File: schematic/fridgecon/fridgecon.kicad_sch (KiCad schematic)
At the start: 3 parts, among them J1 ICSPI, J2 MAX7219, U1 PIC12F675-xP

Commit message: v1.0.0
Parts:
- removed J2: MAX7219, symbol Connector:Conn_01x05_Socket
- added C1: 100n, symbol Device:C
- added D1: 2.2V, symbol Device:D_Zener
- added D2, D3, D5: LED, symbol Device:LED
- added D4: 1N4148, Diode_THT:D_DO-35_SOD27_P7.62mm_Horizontal, symbol Diode:1N4148
- added J2: Motor, symbol Connector:Screw_Terminal_01x02
- added J3: 220V~ IN, symbol Connector:Screw_Terminal_01x02
- added K1: 250V10A, Relay_THT:Relay_SPST-NO_Fujitsu_FTR-LYAA005x_FormA_Vertical, symbol Relay:Fujitsu_FTR-LYAA005x
- added Q1: PNP, symbol Simulation_SPICE:PNP
- added R1, R4: 100, symbol Device:R_US
- added R10, R12, R2, R3, R8, R9: 1K, symbol Device:R_US
- added R11, R6: 44.2K, symbol Device:R_US
- added R5: 220, symbol Device:R_US
- added R7: 13K, symbol Device:R_US
- added RV1: R_Potentiometer_US, symbol Device:R_Potentiometer_US
- added SW1: Tune, symbol Switch:SW_Push
- added U2: LM35-LP, Package_TO_SOT_THT:TO-92_Inline, symbol Sensor_Temperature:LM35-LP
- J1: value ICSPI -> ICSP
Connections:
- net +5V: now also Q1.3 (E), R5.1
- net Relay: now reaches U1.3 (GP4)
- net Relay: now also R9.2
- net Sensor: now reaches U1.5 (GP2)
- net Sensor: now also R3.1, R4.1
- net CS renamed Motor Status
- net Motor Status: now also R8.1
- net Clock renamed PGCLK
- net PGCLK: now also R6.2, R7.1
- net Data renamed PGDATA
- net GND: no longer names the net of U1.8 (VSS)
- net GND: no longer J1.3 (Pin_3)
- net VPP renamed Tune Feedback
- net Tune Feedback: now also R12.1
- new net: D5.2 (A), R12.2
- new net: D1.1 (K), R5.2, R6.1
- new net: C1.1, U2.1 (+V_{S})
- new net: C1.2, R1.2, R2.2
- new net: Q1.2 (B), R9.1
- new net: D2.2 (A), R8.2
- new net: J2.2 (Pin_2), K1.13
- new net: J3.1 (Pin_1), K1.14
- new net: D4.1 (K), K1.A1, Q1.1 (C), R10.1
- new net: D3.1 (K), D4.2 (A), K1.A2
- new net: J2.1 (Pin_1), J3.2 (Pin_2)
- new net: D1.2 (A), R7.2
- new net: R3.2, R4.2
- new net: D3.2 (A), R10.2
- new net: R1.1, U2.2 (V_{OUT})
- new net: R2.1, U2.3 (GND)
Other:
- note added: "ICSP"
- note added: "MCU"
- note added: "Relay"
- note added: "Sensor"
- note added: "User Interface"
- note added: "Voltage Reference"
- moved on the sheet: U1

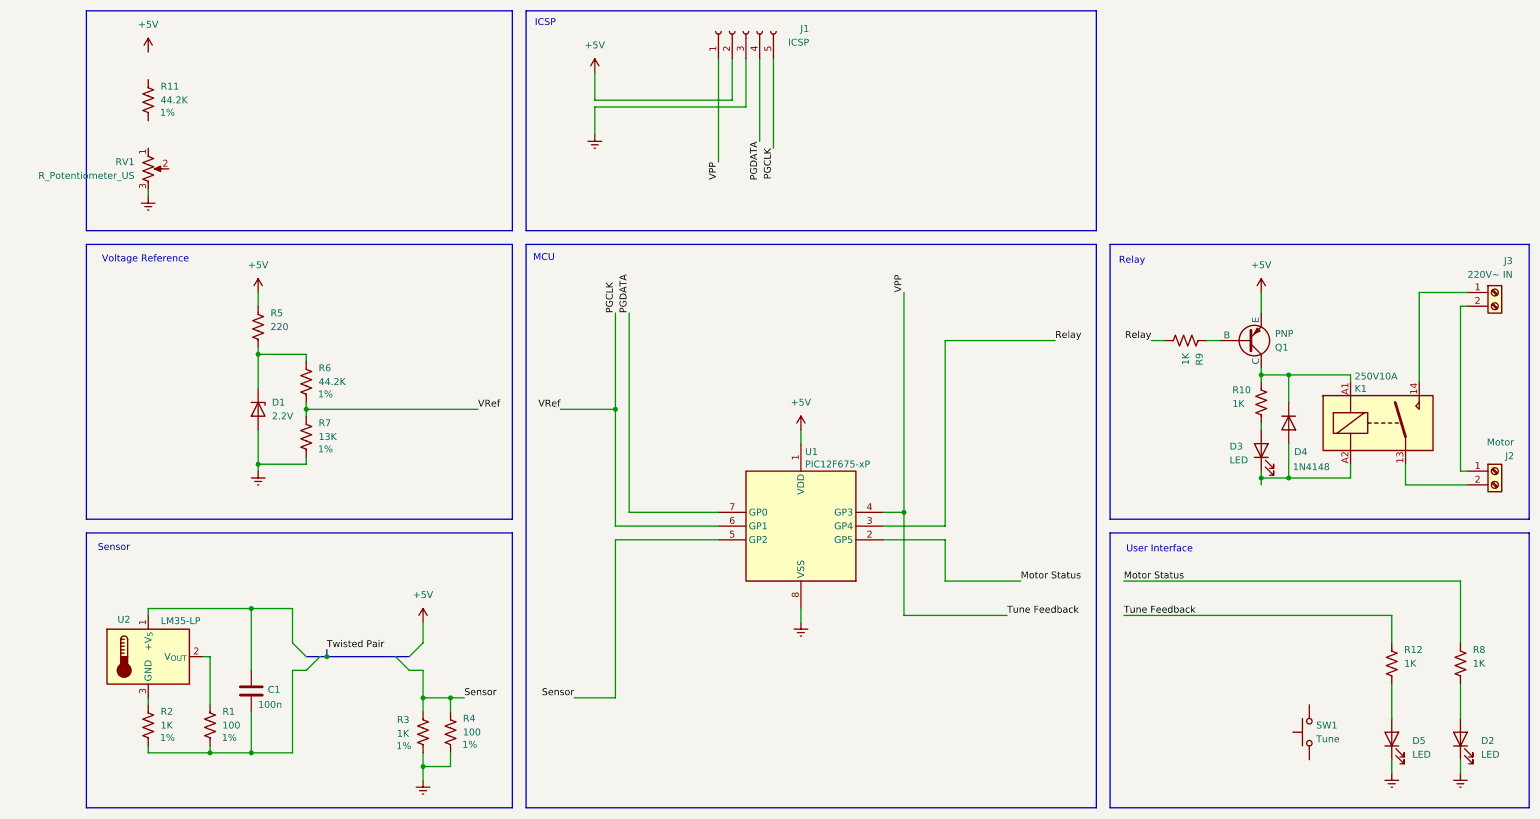
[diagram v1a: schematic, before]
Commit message: feature: GP2/INT
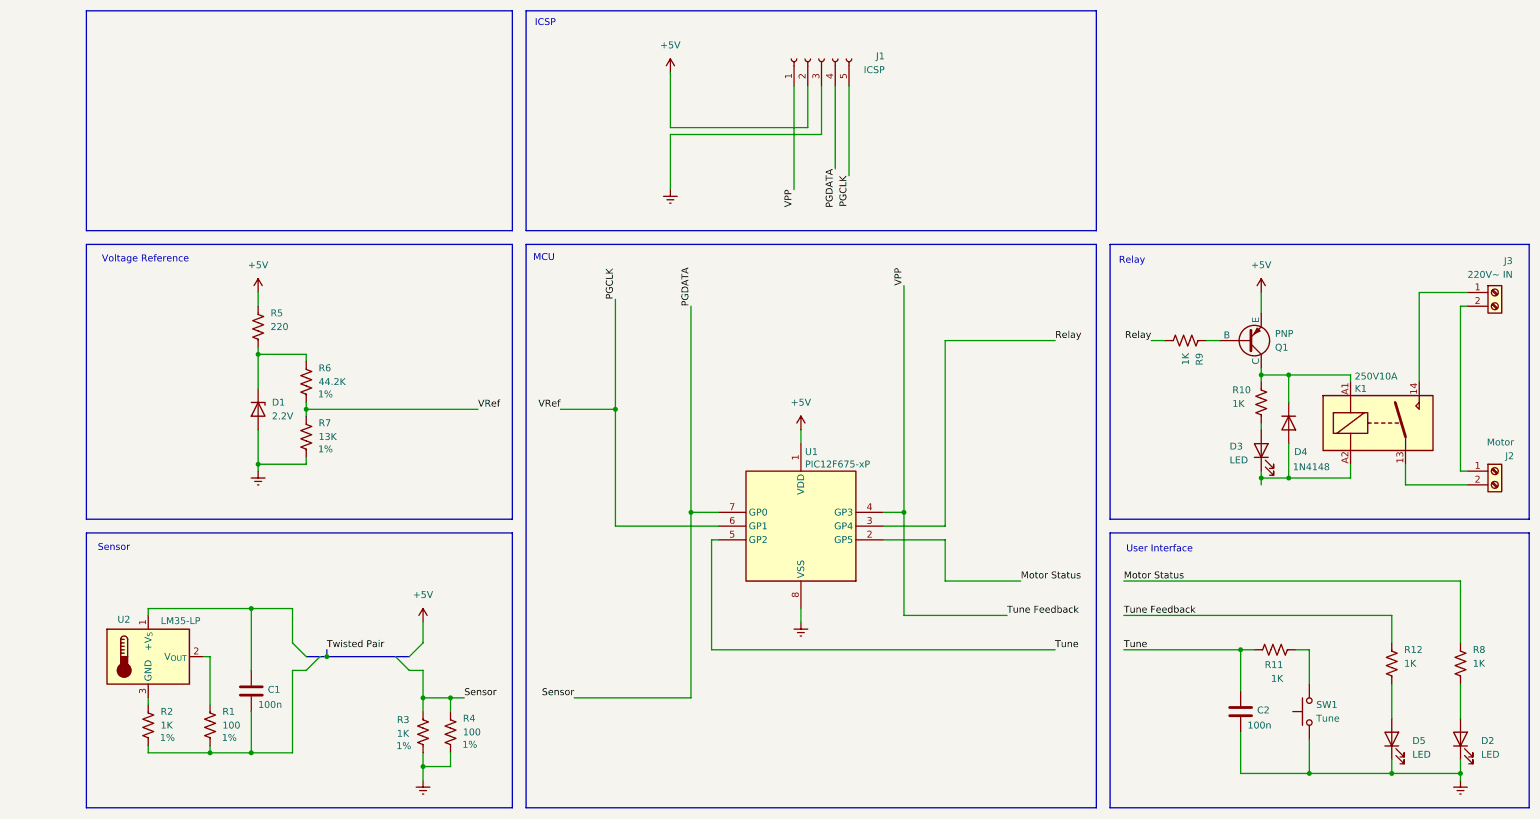
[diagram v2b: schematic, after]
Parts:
- removed RV1: R_Potentiometer_US, symbol Device:R_Potentiometer_US
- added C2: 100n, symbol Device:C
- R11: value 44.2K -> 1K
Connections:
- net PGDATA: now also R3.1, R4.1
- net Tune: now reaches R11.1
- net Tune: now also U1.5 (GP2), C2.1
- net at R11.2: now also SW1.2
- net at D5.1 (K): now also D2.1 (K), SW1.1, C2.2
- removed net Sensor: R3.1, R4.1, U1.5 (GP2)
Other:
- moved on the sheet: J1, SW1

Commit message: Feature: watchdog time
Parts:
- removed D5: LED, symbol Device:LED
- removed R12: 1K, symbol Device:R_US
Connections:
- net Tune Feedback is gone; now on net Tune: J1.1 (Pin_1), U1.4 (GP3)
- net PGDATA: no longer R3.1, R4.1
- net Tune: no longer U1.5 (GP2)
- new net Sensor: R3.1, R4.1, U1.5 (GP2)

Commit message: Feature: schematic
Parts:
- J2: value Motor -> Cooller supply OUT
- J3: value 220V~ IN -> Cooller supply IN
- R11: value 1K -> 100K
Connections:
- net +5V: now also R11.2
- net Tune: now also SW1.2
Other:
- title: (none) -> Mini car refridgerator controller.
- moved on the sheet: C2

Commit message: Final patches
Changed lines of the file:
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@@
+	(symbol
+		(lib_id "power:Earth")
+		(at 232.41 102.87 0)
+		(unit 1)
+		(exclude_from_sim no)
+		(in_bom yes)
+		(on_board yes)
+		(dnp no)
+		(fields_autoplaced yes)
+		(property "Reference" "#PWR11"
+			(at 232.41 109.22 0)
+			(effects
+				(font
+					(size 1.27 1.27)
+				)
+				(hide yes)
+			)
+		)
+		(property "Value" "~"
+			(at 232.41 107.95 0)
+			(effects
+				(font
+					(size 1.27 1.27)
+				)
+			)
+		)
+		(property "Footprint" ""
+			(at 232.41 102.87 0)
+			(effects
+				(font
+					(size 1.27 1.27)
+				)
+				(hide yes)
+			)
+		)
+		(property "Datasheet" "~"
+			(at 232.41 102.87 0)
+			(effects
+				(font
+					(size 1.27 1.27)
+				)
+				(hide yes)
+			)
+		)
+		(property "Description" "Power symbol creates a global label with name \"Earth\""
+			(at 232.41 102.87 0)
+			(effects
+				(font
+					(size 1.27 1.27)
+				)
+				(hide yes)
+			)
+		)
+		(pin "1"
+		)
+		(instances
+			(project "fridgecon"
+				(path "/51ae1284-16dc-47e6-a252-a589b4dac501"
+					(reference "#PWR11")
+					(unit 1)
+				)
+			)
+		)
+	)
 	(symbol
 		(lib_id "power:Earth")
